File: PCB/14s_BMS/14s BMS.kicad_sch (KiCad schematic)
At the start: 0 parts

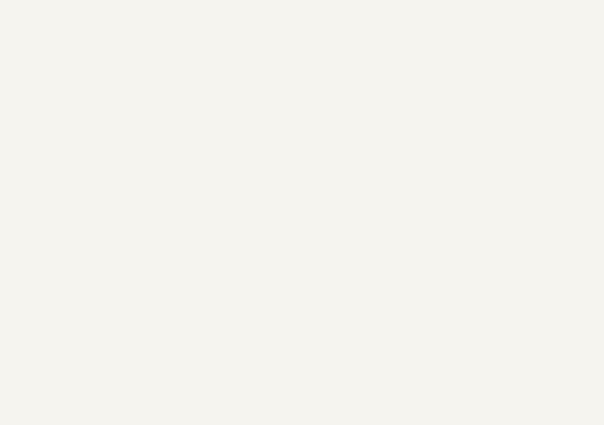
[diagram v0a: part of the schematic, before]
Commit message: started on power supply circuitry
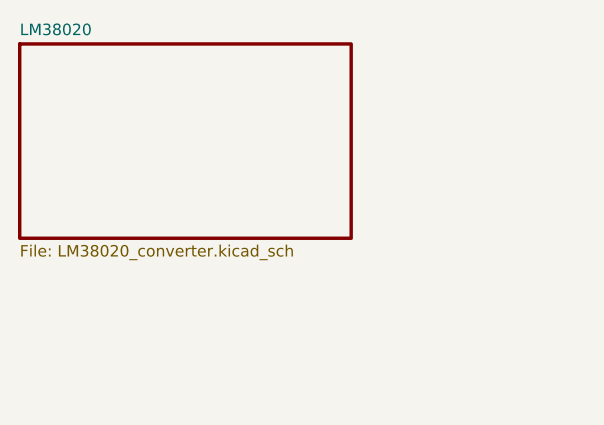
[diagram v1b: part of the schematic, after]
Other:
- added sheet LM38020 (LM38020_converter.kicad_sch)
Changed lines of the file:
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@@
 	(paper "A3")
+	(sheet
+		(at 43.18 49.53)
+		(size 36.83 21.59)
+		(fields_autoplaced yes)
+		(stroke
+			(width 0.381)
+			(type solid)
+		)
+		(fill
+			(color 0 0 0 0.0000)
+		)
+		(property "Sheetname" "LM38020"
+			(at 43.18 48.7041 0)
+			(effects
+				(font
+					(size 1.27 1.27)
+				)
+				(justify left bottom)
+			)
+		)
+		(property "Sheetfile" "LM38020_converter.kicad_sch"
+			(at 43.18 71.8189 0)
+			(effects
+				(font
+					(size 1.27 1.27)
+				)
+				(justify left top)
+			)
+		)
+		(instances
+			(project "14s BMS"
+				(path "/e0335a39-2917-4993-8bc8-e5e4f72c0f3a"
+					(page "4")
+				)
+			)
+		)
+	)
 	(sheet
 		(at 133.35 105.41)

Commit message: rev 1 of power supply design
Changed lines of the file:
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@@
 	(generator "eeschema")
 	(generator_version "8.0")
-	(paper "A3")
+	(paper "A4")
 	(sheet
-		(at 43.18 49.53)
-		(size 36.83 21.59)
+		(at 22.86 72.39)
+		(size 44.45 38.1)
 		(fields_autoplaced yes)
 		(stroke
@@
 		)
 		(property "Sheetname" "LM38020"
-			(at 43.18 48.7041 0)
+			(at 22.86 71.5641 0)
 			(effects
 				(font
@@
 		)
 		(property "Sheetfile" "LM38020_converter.kicad_sch"
-			(at 43.18 71.8189 0)
+			(at 22.86 111.1889 0)
 			(effects
 				(font
@@
 	)
 	(sheet
-		(at 133.35 105.41)
-		(size 41.91 33.02)
+		(at 113.03 74.93)
+		(size 54.61 44.45)
 		(fields_autoplaced yes)
 		(stroke
@@
 		)
 		(property "Sheetname" "MCU_etc"
-			(at 133.35 104.6984 0)
+			(at 113.03 74.2184 0)
 			(effects
 				(font
@@
 		)
 		(property "Sheetfile" "ESP_32_breakout.kicad_sch"
-			(at 133.35 139.0146 0)
+			(at 113.03 119.9646 0)
 			(effects
 				(font
@@
 	)
 	(sheet
-		(at 237.49 105.41)
+		(at 196.85 80.01)
 		(size 48.26 35.56)
 		(fields_autoplaced yes)
@@
 		)
 		(property "Sheetname" "LTC6813"
-			(at 237.49 104.6984 0)
+			(at 196.85 79.2984 0)
 			(effects
 				(font
@@
 		)
 		(property "Sheetfile" "LTC6813-1_breakout.kicad_sch"
-			(at 237.49 141.5546 0)
+			(at 196.85 116.1546 0)
 			(effects
 				(font
